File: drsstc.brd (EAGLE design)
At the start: 99.1 x 99.1 mm, 122 parts, among them U1 AP1501, U10 LM311, U11 74HC74, U12 LM8365, U13 ICM7216D, U14 ICM7216D, U2 74AHCT1G32, U3 AP1506, U4 MCP4706, U5 UCC27423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

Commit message: Updating DRSSTC board to Rev B
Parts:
- removed CNTRL: (no value), pinhead:1X06
- added MODE, MSTR, TEST, TRIG: (no value), pinhead:1X02
- R15: device resistor:R1206 -> drsstc:RESAD1560W80L1200D400B
- TP2: device pinhead:1X04 -> pinhead:1X06
- moved R15 3.83 mm to (18.8, 24.0), flipped to the bottom, turned to 180 degrees
- moved TP2 2.82 mm to (27.2, 54.2)
- moved I2C 1.78 mm to (93.0, 52.8)
- moved C1 0.13 mm to (65.8, 65.0)
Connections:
- removed net MODE1: CNTRL.3, JP5.19, R2.1
- removed net MODE2: CNTRL.4, JP5.18, R3.1
- removed net N$26: D4.C, D5.A, R14.1, TP2.1, U6.3
- removed net POT: CNTRL.2, JP5.20, R1.1
- new net FB_IN: D4.C, D5.A, R14.1, TP2.2, U6.3
- new net MODE: JP5.18, MODE.1, R3.1
- new net TEST: JP5.19, R2.1, TEST.1
- new net TRIG: JP5.20, R1.1, TRIG.1
- net ACTIVE: now also TP2.6
- net GND: now also NEOPIXEL.3, TP2.1, U2.3, U6.5; no longer CNTRL.1, NEOPIXEL.2, TP2.2, U2.5, U6.1
- net INA: now also TP2.5
- net MSTR_EN: now also MSTR.1; no longer CNTRL.5
- net N$13: now also NEOPIXEL.2; no longer NEOPIXEL.3
- net VCC: now also MODE.2, MSTR.2, TEST.2, TRIG.2, U2.5, U6.1; no longer CNTRL.6, U2.3, U6.5
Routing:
- net FB_IN: track 0.00 -> 27.9 mm, vias 0 -> 1
- net N$26: track 25.0 -> 0.00 mm
- net INA: track 44.6 -> 61.4 mm
- net MODE: track 0.00 -> 14.5 mm
- net MODE2: track 14.2 -> 0.00 mm
- net TEST: track 0.00 -> 14.1 mm
- net MODE1: track 14.0 -> 0.00 mm
- net POT: track 13.8 -> 0.00 mm
- net TRIG: track 0.00 -> 10.3 mm
- net VCC: track 58.7 -> 65.6 mm
- net ACTIVE: track 43.3 -> 48.7 mm
- net UVLO: track 30.0 -> 34.3 mm
- net N$20: track 46.2 -> 43.1 mm
- net GND: track 49.9 -> 47.9 mm, vias 10 -> 11
- net PRIMARY: track 108.7 -> 106.8 mm, vias 1 -> 2
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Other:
- board text added: "ACTV"
- board text added: "DRSSTC DRIVER Rev B"
- board text added: "INA"
- board text added: "PRI"
- board text added: "UV"
- board text removed: "A1"
- board text removed: "A2"
- board text removed: "A3"
- board text removed: "DRSSTC DRIVER Rev A"
- board text removed: "MSTR"
- board text removed: "OCD TP"
- board text removed: "PRIM"

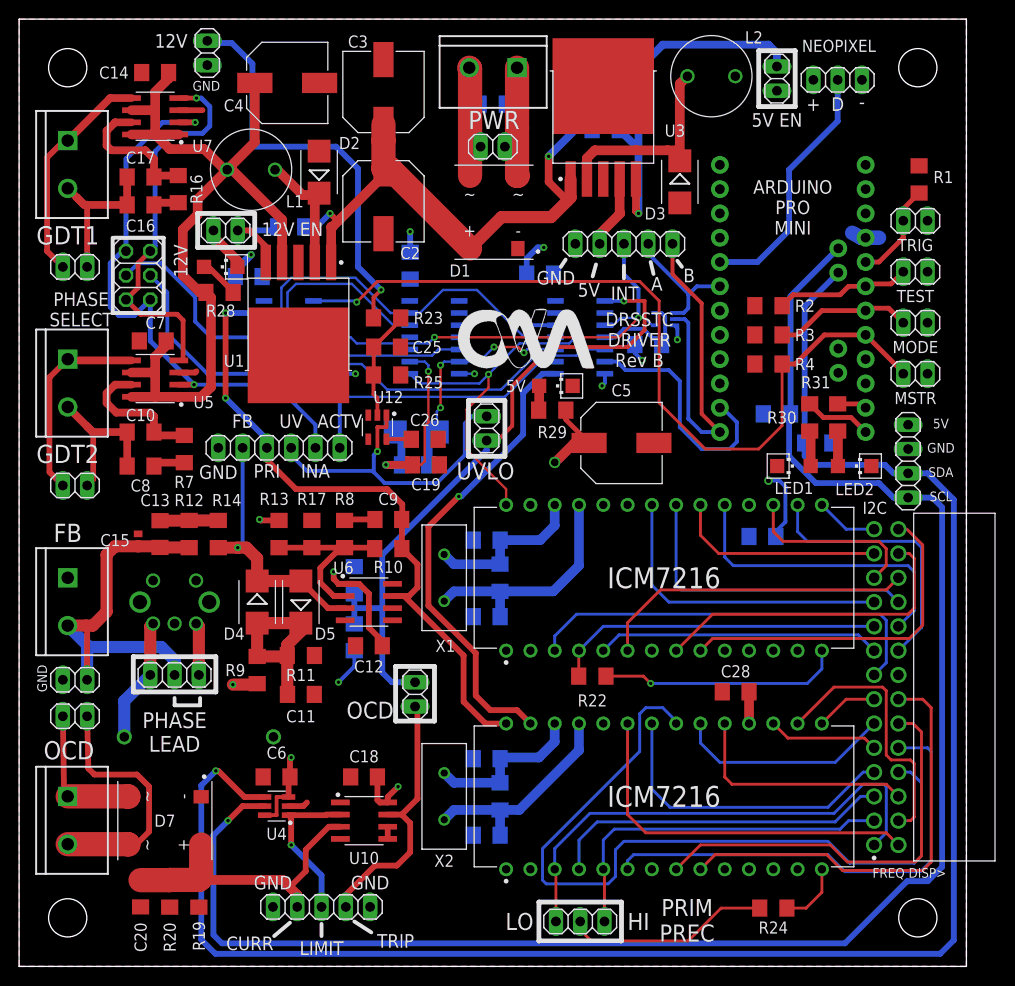
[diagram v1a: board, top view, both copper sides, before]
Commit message: Updating Rev B board, linking freq counter to driver input signal
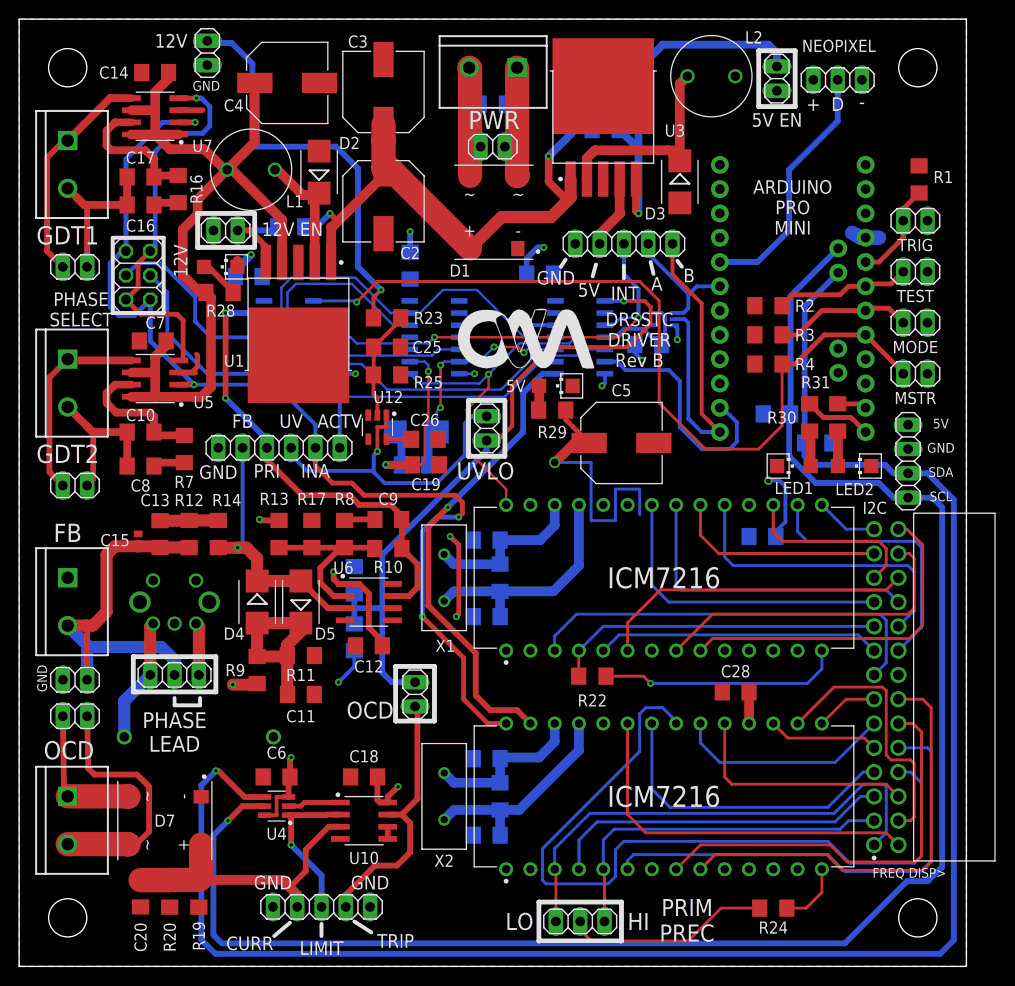
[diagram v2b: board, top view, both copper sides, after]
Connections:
- net INA: now also U14.28
- net PRIMARY: no longer U14.28
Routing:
- net INA: track 61.4 -> 111.2 mm, vias 2 -> 4
- net VCC: track 65.6 -> 94.0 mm, vias 6 -> 8
- net PRIMARY: track 106.8 -> 87.0 mm
- net GND: track 47.9 -> 49.4 mm
- net N$5: track 69.6 -> 70.2 mm
